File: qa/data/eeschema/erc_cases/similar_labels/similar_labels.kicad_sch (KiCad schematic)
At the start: 0 parts

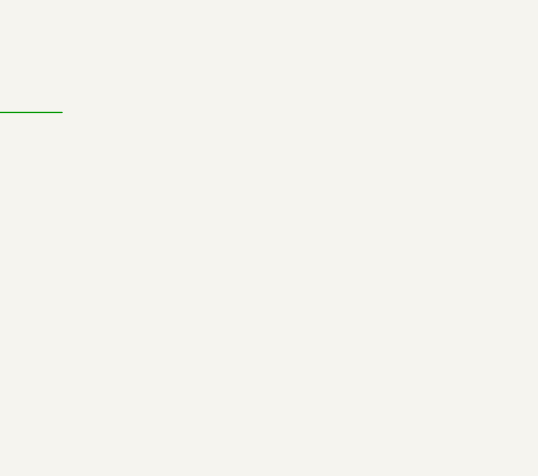
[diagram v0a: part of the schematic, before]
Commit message: qa: extend four ERC fixtures to reach what the S2-4b-7/8 sweep found unpinned
similar_labels gains a subsheet with a local daTa (case variants on two sheets are fine),
similar_power an ordinary part valued gnd (only power pins compare), symbol_pins a twin
whose duplicate pin numbers are jumpers, footprints a unit with no footprint and a
Resistor_SMD:R_* filter (a ':' filter matches the whole id). kicad-cli regenerated
every report; all match.

Co-Authored-By: Claude Opus 5.5 (1M context) <noreply@anthropic.com>
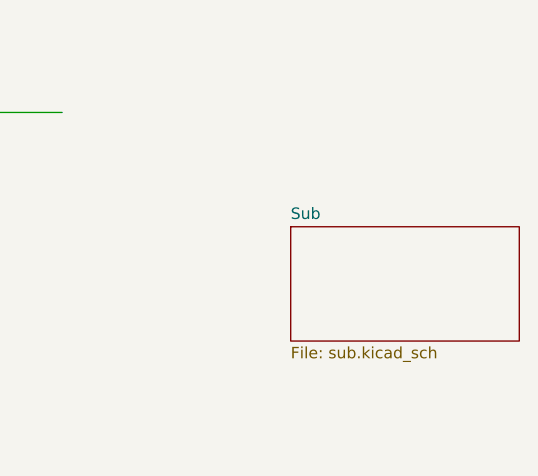
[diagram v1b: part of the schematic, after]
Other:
- added sheet Sub (sub.kicad_sch)
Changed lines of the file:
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@@
 	(wire (pts (xy 50.8 101.6) (xy 76.2 101.6)) (stroke (width 0) (type default)))
 	(label "same" (at 63.5 101.6 0) (effects (font (size 1.27 1.27)) (justify left bottom)))
+	(sheet (at 152.4 76.2) (size 25.4 12.7) (fields_autoplaced yes)
+		(stroke (width 0.1524) (type solid)) (fill (color 0 0 0 0.0000))
+		(property "Sheetname" "Sub" (at 152.4 75.4884 0) (effects (font (size 1.27 1.27)) (justify left bottom)))
+		(property "Sheetfile" "sub.kicad_sch" (at 152.4 89.4846 0) (effects (font (size 1.27 1.27)) (justify left top)))
+		(instances (project "similar_labels" (path "/21111111-2222-3333-4444-555555555555" (page "2"))))
+	)
 	(sheet_instances (path "/" (page "1")))
 )
